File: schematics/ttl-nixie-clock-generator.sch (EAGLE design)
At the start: 10 parts, among them IC1 7400N, Q1 1MHz

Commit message: schenatics: ttl-generator: protoboard version
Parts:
- added CLK_OUT, GND, VCC: (no value), wirepad:2,15/1,0
- C2: device capacitor-wima:C5/3 -> capacitor-wima:C15/5
- Q1: device crystal:CRYSTALHC49U-V -> crystal:CRYSTALHC33U-V
- R3, R4, R5, R6: device resistor:R-EU_0207/5V -> resistor:R-EU_0207/12
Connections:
- removed net GEN_OUT: IC1D.O
- new net CLK_OUT: CLK_OUT.P, IC1D.O
- new net VCC: VCC.P
- net GND: now also GND.P
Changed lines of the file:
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@@
 <setting verticaltext="up"/>
 </settings>
-<grid distance="0.1" unitdist="inch" unit="inch" style="lines" multiple="1" display="yes" altdistance="0.01" altunitdist="inch" altunit="inch"/>
+<grid distance="0.1" unitdist="inch" unit="inch" style="lines" multiple="1" display="no" altdistance="0.01" altunitdist="inch" altunit="inch"/>
 <layers>
-<layer number="1" name="Top" color="4" fill="1" visible="no" active="no"/>
-<layer number="16" name="Bottom" color="1" fill="1" visible="no" active="no"/>
-<layer number="17" name="Pads" color="2" fill="1" visible="no" active="no"/>
-<layer number="18" name="Vias" color="2" fill="1" visible="no" active="no"/>
-<layer number="19" name="Unrouted" color="6" fill="1" visible="no" active="no"/>
-<layer number="20" name="Dimension" color="15" fill="1" visible="no" active="no"/>
-<layer number="21" name="tPlace" color="7" fill="1" visible="no" active="no"/>
-<layer number="22" name="bPlace" color="7" fill="1" visible="no" active="no"/>
-<layer number="23" name="tOrigins" color="15" fill="1" visible="no" active="no"/>
-<layer number="24" name="bOrigins" color="15" fill="1" visible="no" active="no"/>
-<layer number="25" name="tNames" color="7" fill="1" visible="no" active="no"/>
-<layer number="26" name="bNames" color="7" fill="1" visible="no" active="no"/>
-<layer number="27" name="tValues" color="7" fill="1" visible="no" active="no"/>
-<layer number="28" name="bValues" color="7" fill="1" visible="no" active="no"/>
+<layer number="1" name="Top" color="4" fill="1" visible="yes" active="no"/>
+<layer number="16" name="Bottom" color="1" fill="1" visible="yes" active="no"/>
+<layer number="17" name="Pads" color="2" fill="1" visible="yes" active="no"/>
+<layer number="18" name="Vias" color="2" fill="1" visible="yes" active="no"/>
+<layer number="19" name="Unrouted" color="6" fill="1" visible="yes" active="no"/>
+<layer number="20" name="Dimension" color="15" fill="1" visible="yes" active="no"/>
+<layer number="21" name="tPlace" color="7" fill="1" visible="yes" active="no"/>
+<layer number="22" name="bPlace" color="7" fill="1" visible="yes" active="no"/>
+<layer number="23" name="tOrigins" color="15" fill="1" visible="yes" active="no"/>
+<layer number="24" name="bOrigins" color="15" fill="1" visible="yes" active="no"/>
+<layer number="25" name="tNames" color="7" fill="1" visible="yes" active="no"/>
+<layer number="26" name="bNames" color="7" fill="1" visible="yes" active="no"/>
+<layer number="27" name="tValues" color="7" fill="1" visible="yes" active="no"/>
+<layer number="28" name="bValues" color="7" fill="1" visible="yes" active="no"/>
 <layer number="29" name="tStop" color="7" fill="3" visible="no" active="no"/>
 <layer number="30" name="bStop" color="7" fill="6" visible="no" active="no"/>
@@
 <layer number="35" name="tGlue" color="7" fill="4" visible="no" active="no"/>
 <layer number="36" name="bGlue" color="7" fill="5" visible="no" active="no"/>
-<layer number="37" name="tTest" color="7" fill="1" visible="no" active="no"/>
-<layer number="38" name="bTest" color="7" fill="1" visible="no" active="no"/>
+<layer number="37" name="tTest" color="7" fill="1" visible="yes" active="no"/>
+<layer number="38" name="bTest" color="7" fill="1" visible="yes" active="no"/>
 <layer number="39" name="tKeepout" color="4" fill="11" visible="no" active="no"/>
 <layer number="40" name="bKeepout" color="1" fill="11" visible="no" active="no"/>
@@
 <layer number="44" name="Drills" color="7" fill="1" visible="no" active="no"/>
 <layer number="45" name="Holes" color="7" fill="1" visible="no" active="no"/>
-<layer number="46" name="Milling" color="3" fill="1" visible="no" active="no"/>
-<layer number="47" name="Measures" color="7" fill="1" visible="no" active="no"/>
-<layer number="48" name="Document" color="7" fill="1" visible="no" active="no"/>
-<layer number="49" name="Reference" color="7" fill="1" visible="no" active="no"/>
-<layer number="50" name="dxf" color="7" fill="1" visible="no" active="no"/>
-<layer number="51" name="tDocu" color="7" fill="1" visible="no" active="no"/>
-<layer number="52" name="bDocu" color="7" fill="1" visible="no" active="no"/>
-<layer number="53" name="tGND_GNDA" color="7" fill="9" visible="no" active="no"/>
-<layer number="54" name="bGND_GNDA" color="1" fill="9" visible="no" active="no"/>
-<layer number="56" name="wert" color="7" fill="1" visible="no" active="no"/>
-<layer number="57" name="tCAD" color="7" fill="1" visible="no" active="no"/>
+<layer number="46" name="Milling" color="3" fill="1" visible="yes" active="no"/>
+<layer number="47" name="Measures" color="7" fill="1" visible="yes" active="no"/>
+<layer number="48" name="Document" color="7" fill="1" visible="yes" active="no"/>
+<layer number="49" name="Reference" color="7" fill="1" visible="yes" active="no"/>
+<layer number="50" name="dxf" color="7" fill="1" visible="yes" active="no"/>
+<layer number="51" name="tDocu" color="7" fill="1" visible="yes" active="no"/>
+<layer number="52" name="bDocu" color="7" fill="1" visible="yes" active="no"/>
+<layer number="53" name="tGND_GNDA" color="7" fill="9" visible="yes" active="no"/>
+<layer number="54" name="bGND_GNDA" color="1" fill="9" visible="yes" active="no"/>
+<layer number="56" name="wert" color="7" fill="1" visible="yes" active="no"/>
+<layer number="57" name="tCAD" color="7" fill="1" visible="yes" active="no"/>
 <layer number="90" name="Modules" color="5" fill="1" visible="yes" active="yes"/>
 <layer number="91" name="Nets" color="2" fill="1" visible="yes" active="yes"/>
@@
 <part name="R1" library="varistor" deviceset="VARISTOR" device="-7,5" value="12J"/>
 <part name="R2" library="varistor" deviceset="VARISTOR" device="-7,5" value="12J"/>
-<part name="Q1" library="crystal" deviceset="CRYSTAL" device="HC49U-V" value="1MHz"/>
-<part name="C2" library="capacitor-wima" deviceset="C" device="5/3" value="1nF"/>
+<part name="Q1" library="crystal" deviceset="CRYSTAL" device="HC33U-V" value="1MHz"/>
+<part name="C2" library="capacitor-wima" deviceset="C" device="15/5" value="1nF"/>
 <part name="C3" library="resistor" deviceset="C-TRIMM" device="808-7.5" value="2/7pF"/>
-<part name="R3" library="resistor" deviceset="R-EU_" device="0207/5V" value="1K2"/>
-<part name="R4" library="resistor" deviceset="R-EU_" device="0207/5V" value="1K2"/>
-<part name="R5" library="resistor" deviceset="R-EU_" device="0207/5V" value="2K2"/>
-<part name="R6" library="resistor" deviceset="R-EU_" device="0207/5V" value="2K2"/>
+<part name="R3" library="resistor" deviceset="R-EU_" device="0207/12" value="1K2"/>
+<part name="R4" library="resistor" deviceset="R-EU_" device="0207/12" value="1K2"/>
+<part name="R5" library="resistor" deviceset="R-EU_" device="0207/12" value="2K2"/>
+<part name="R6" library="resistor" deviceset="R-EU_" device="0207/12" value="2K2"/>
 <part name="GND1" library="SparkFun-Aesthetics" deviceset="GND" device=""/>
 <part name="GND2" library="SparkFun-Aesthetics" deviceset="GND" device=""/>
 <part name="SUPPLY2" library="SparkFun-Aesthetics" deviceset="VCC" device=""/>
+<part name="VCC" library="wirepad" deviceset="2,15/1,0" device=""/>
+<part name="GND" library="wirepad" deviceset="2,15/1,0" device=""/>
+<part name="GND3" library="SparkFun-Aesthetics" deviceset="GND" device=""/>
+<part name="CLK_OUT" library="wirepad" deviceset="2,15/1,0" device=""/>
 </parts>
 <sheets>
@@
 <instance part="GND1" gate="1" x="-15.24" y="27.94"/>
 <instance part="GND2" gate="1" x="17.78" y="27.94"/>
-<instance part="SUPPLY2" gate="G$1" x="68.58" y="76.2"/>
+<instance part="SUPPLY2" gate="G$1" x="68.58" y="81.28"/>
+<instance part="VCC" gate="1" x="63.5" y="78.74"/>
+<instance part="GND" gate="1" x="63.5" y="68.58"/>
+<instance part="GND3" gate="1" x="68.58" y="63.5"/>
+<instance part="CLK_OUT" gate="1" x="63.5" y="73.66"/>
 </instances>
 <busses>
@@
 <wire x1="17.78" y1="33.02" x2="17.78" y2="30.48" width="0.1524" layer="91"/>
 </segment>
+<segment>
+<pinref part="GND" gate="1" pin="P"/>
+<pinref part="GND3" gate="1" pin="GND"/>
+<wire x1="66.04" y1="68.58" x2="68.58" y2="68.58" width="0.1524" layer="91"/>
+<wire x1="68.58" y1="68.58" x2="68.58" y2="66.04" width="0.1524" layer="91"/>
+</segment>
 </net>
 <net name="N$3" class="0">
@@
 </segment>
 </net>
-<net name="GEN_OUT" class="0">
+<net name="CLK_OUT" class="0">
 <segment>
 <pinref part="IC1" gate="D" pin="O"/>
@@
 <label x="86.36" y="50.8" size="1.778" layer="95" xref="yes"/>
 </segment>
+<segment>
+<pinref part="CLK_OUT" gate="1" pin="P"/>
+<wire x1="66.04" y1="73.66" x2="68.58" y2="73.66" width="0.1524" layer="91"/>
+<label x="68.58" y="73.66" size="1.778" layer="95" xref="yes"/>
+</segment>
 </net>
 <net name="VCC" class="0">
 <segment>
 <pinref part="SUPPLY2" gate="G$1" pin="VCC"/>
-<wire x1="68.58" y1="73.66" x2="68.58" y2="76.2" width="0.1524" layer="91"/>
-<label x="68.58" y="73.66" size="1.778" layer="95" rot="R270" xref="yes"/>
-</segment>
-</net>
+<wire x1="68.58" y1="78.74" x2="68.58" y2="81.28" width="0.1524" layer="91"/>
+<pinref part="VCC" gate="1" pin="P"/>
+<wire x1="68.58" y1="78.74" x2="66.04" y2="78.74" width="0.1524" layer="91"/>
+</segment>
+</net>

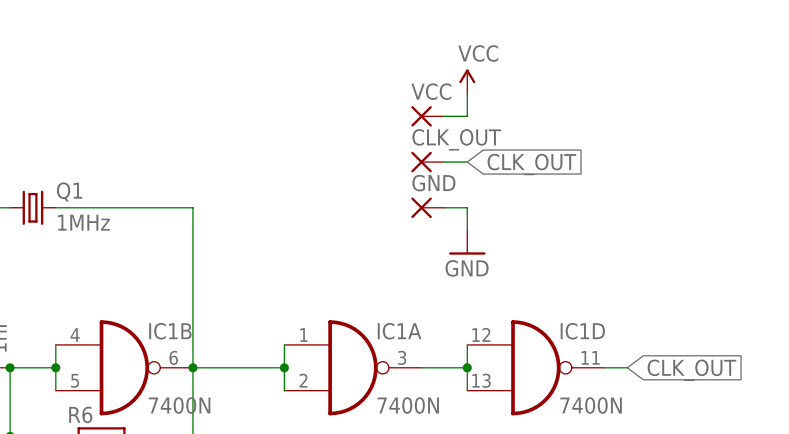
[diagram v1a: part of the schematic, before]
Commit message: ttl-generator: protoboard built version
The version i built on protoboard, it works!
The multimeter says 999.7 kHz :)
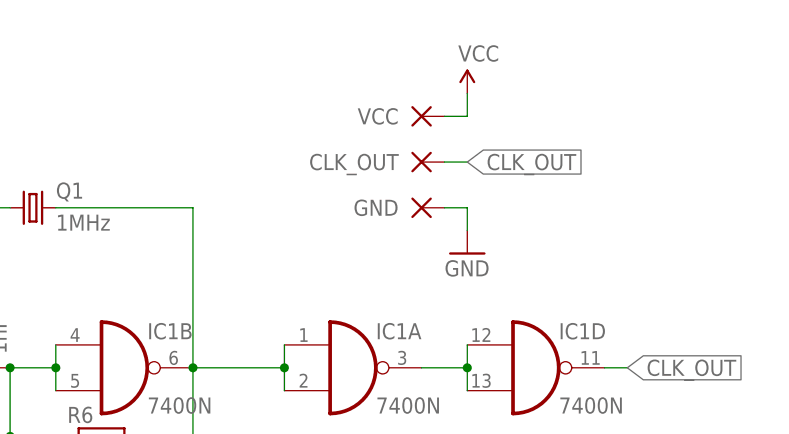
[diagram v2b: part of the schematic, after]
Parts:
- CLK_OUT: value (none) -> CLK_OUT
- GND: value (none) -> GND
- VCC: value (none) -> VCC
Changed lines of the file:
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@@
 <part name="GND2" library="SparkFun-Aesthetics" deviceset="GND" device=""/>
 <part name="SUPPLY2" library="SparkFun-Aesthetics" deviceset="VCC" device=""/>
-<part name="VCC" library="wirepad" deviceset="2,15/1,0" device=""/>
-<part name="GND" library="wirepad" deviceset="2,15/1,0" device=""/>
+<part name="VCC" library="wirepad" deviceset="2,15/1,0" device="" value="VCC"/>
+<part name="GND" library="wirepad" deviceset="2,15/1,0" device="" value="GND"/>
 <part name="GND3" library="SparkFun-Aesthetics" deviceset="GND" device=""/>
-<part name="CLK_OUT" library="wirepad" deviceset="2,15/1,0" device=""/>
+<part name="CLK_OUT" library="wirepad" deviceset="2,15/1,0" device="" value="CLK_OUT"/>
 </parts>
 <sheets>
@@
 <instance part="GND2" gate="1" x="17.78" y="27.94"/>
 <instance part="SUPPLY2" gate="G$1" x="68.58" y="81.28"/>
-<instance part="VCC" gate="1" x="63.5" y="78.74"/>
-<instance part="GND" gate="1" x="63.5" y="68.58"/>
+<instance part="VCC" gate="1" x="63.5" y="78.74" smashed="yes">
+<attribute name="NAME" x="60.96" y="78.74" size="1.778" layer="95" align="center-right"/>
+</instance>
+<instance part="GND" gate="1" x="63.5" y="68.58" smashed="yes">
+<attribute name="NAME" x="60.96" y="68.58" size="1.778" layer="95" align="center-right"/>
+</instance>
 <instance part="GND3" gate="1" x="68.58" y="63.5"/>
-<instance part="CLK_OUT" gate="1" x="63.5" y="73.66"/>
+<instance part="CLK_OUT" gate="1" x="63.5" y="73.66" smashed="yes">
+<attribute name="NAME" x="60.96" y="73.66" size="1.778" layer="95" align="center-right"/>
+</instance>
 </instances>
 <busses>

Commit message: nixie-clock-generator: added divide circuit, prettify
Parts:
- added CLK_1HZ: VCC, wirepad:2,15/1,0
- added IC2, IC3, IC4, IC5, IC6, IC8: 74LS93N, 74xx-eu:74LS93N
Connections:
- removed net CLK_OUT: CLK_OUT.P, IC1D.O
- new net CLK_1HZ: CLK_1HZ.P, IC8A.QD, IC8A.R0(1)
- new net CLK_1MHZ: CLK_OUT.P, IC1D.O, IC2A.CKA
- new net N$10: IC5A.QD, IC5A.R0(1), IC6A.CKA
- new net N$11: IC6A.CKB, IC6A.QA
- new net N$12: IC6A.QB, IC6A.R0(2)
- new net N$13: IC6A.QD, IC6A.R0(1), IC8A.CKA
- new net N$14: IC8A.CKB, IC8A.QA
- new net N$15: IC8A.QB, IC8A.R0(2)
- new net N$16: IC2A.CKB, IC2A.QA
- new net N$17: IC2A.QD, IC2A.R0(1), IC3A.CKA
- new net N$18: IC2A.QB, IC2A.R0(2)
- new net N$19: IC3A.QB, IC3A.R0(2)
- new net N$20: IC3A.QD, IC3A.R0(1), IC4A.CKA
- new net N$21: IC3A.CKB, IC3A.QA
- new net N$22: IC4A.CKB, IC4A.QA
- new net N$23: IC4A.QB, IC4A.R0(2)
- new net N$24: IC4A.QD, IC4A.R0(1), IC5A.CKA
- new net N$8: IC5A.CKB, IC5A.QA
- new net N$9: IC5A.QB, IC5A.R0(2)
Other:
- note added: "CLOCK DIVIDER 1MHz -> 1Hz"
- note added: "CLOCK GENERATOR (1MHz)"
- note added: "divide-by-10: out: 1 Hz"
- note added: "divide-by-10: out: 1 kHz"
- note added: "divide-by-10: out: 10 Hz"
- note added: "divide-by-10: out: 10 kHz"
- note added: "divide-by-10: out: 100 Hz"
- note added: "divide-by-10: out: 100 kHz"
- moved on the sheet: C2, C3, CLK_OUT, GND, IC1A, IC1B, IC1C, IC1D, Q1, R1, R2, R3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
